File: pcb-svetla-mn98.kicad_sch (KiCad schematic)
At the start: 7 parts, among them J1 TURN PAIRS, J14 P6DC INPUT, J2 MAIN LIGHTS, J3 AUX LIGHTS

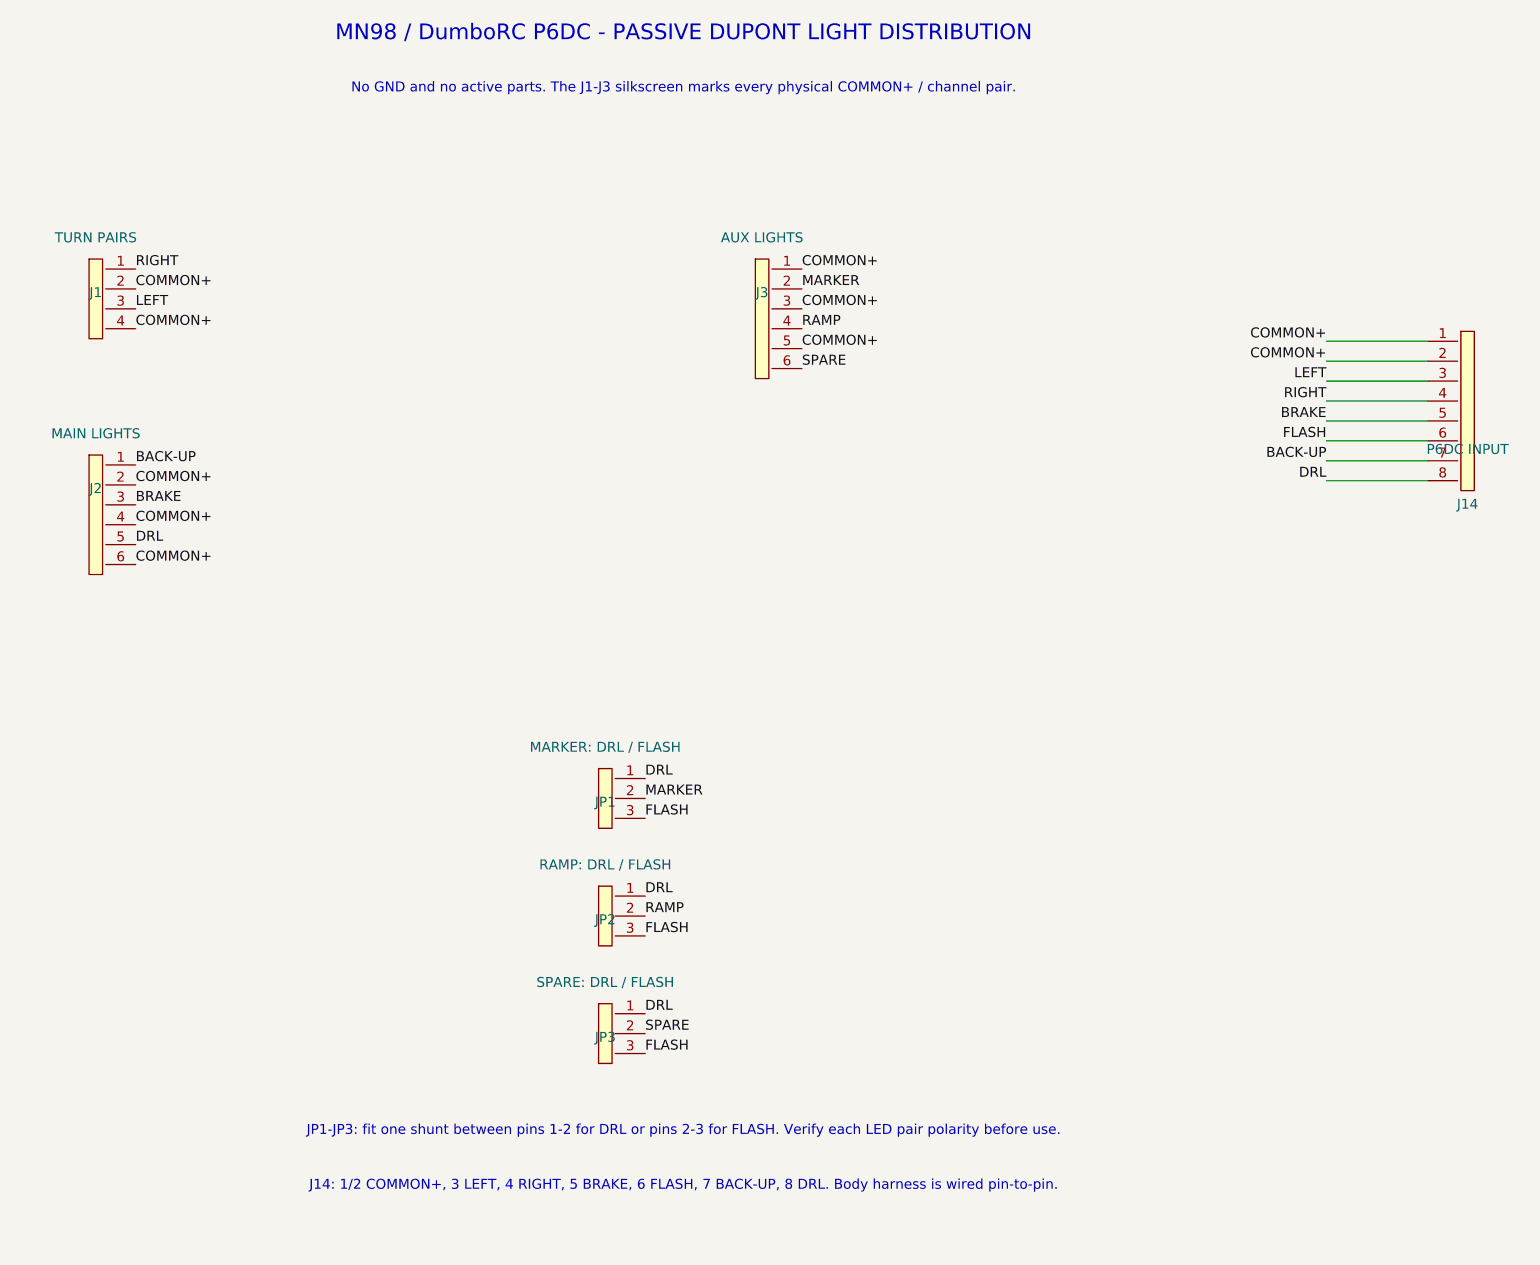
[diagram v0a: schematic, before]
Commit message: Revise body distributor placement
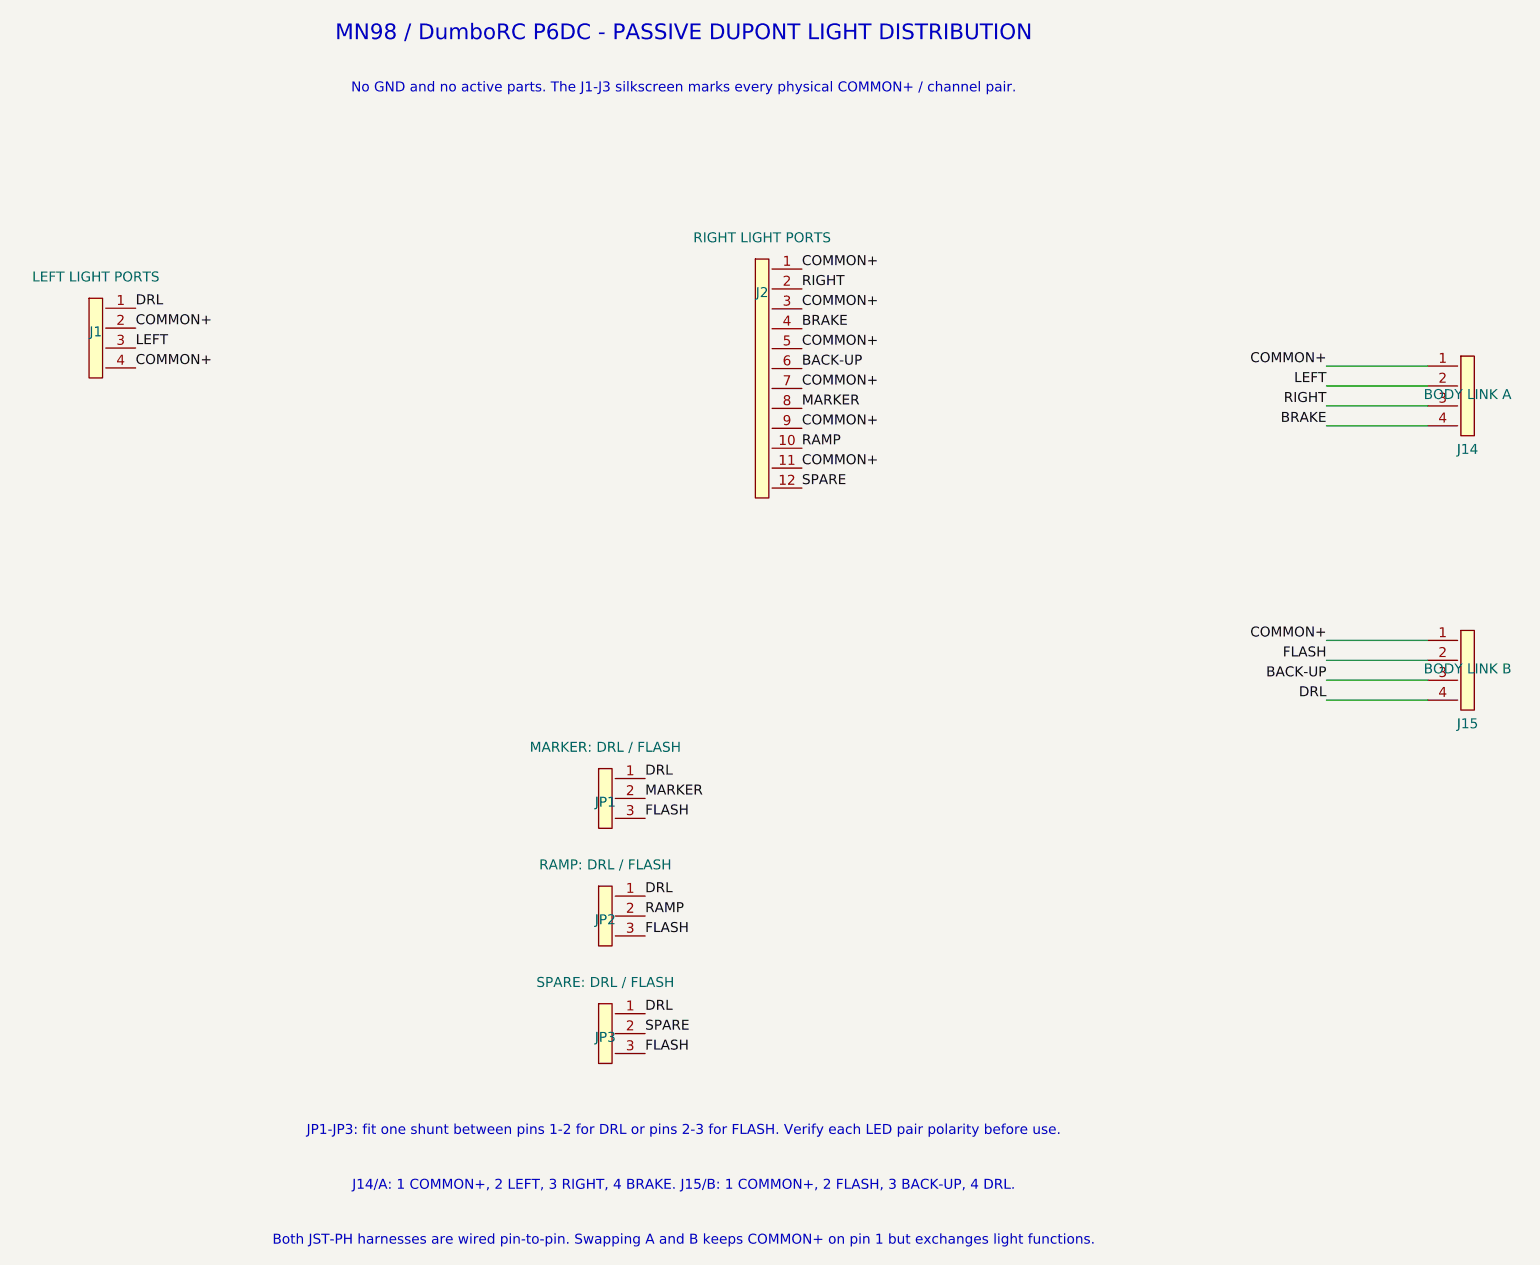
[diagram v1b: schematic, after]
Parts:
- removed J3: AUX LIGHTS, Connector_PinHeader_2.54mm:PinHeader_1x06_P2.54mm_Horizontal, symbol MN98:Conn_01x06
- added J15: BODY LINK B, Connector_JST:JST_PH_S4B-PH-K_1x04_P2.00mm_Horizontal, symbol MN98:Conn_01x04_Input
- J1: value TURN PAIRS -> LEFT LIGHT PORTS
- J14: value P6DC INPUT -> BODY LINK A; footprint Connector_JST:JST_XH_S8B-XH-A_1x08_P2.50mm_Horizontal -> Connector_JST:JST_PH_S4B-PH-K_1x04_P2.00mm_Horizontal; symbol MN98:Conn_01x08_Input -> MN98:Conn_01x04_Input
- J2: value MAIN LIGHTS -> RIGHT LIGHT PORTS; footprint Connector_PinHeader_2.54mm:PinHeader_1x06_P2.54mm_Horizontal -> Connector_PinHeader_2.54mm:PinHeader_1x12_P2.54mm_Horizontal; symbol MN98:Conn_01x06 -> MN98:Conn_01x12
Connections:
- net BACK-UP: now also J2.6 (Pin_6), J15.3 (Pin_3); no longer J14.7 (Pin_7), J2.1 (Pin_1)
- net BRAKE: now also J14.4 (Pin_4), J2.4 (Pin_4); no longer J14.5 (Pin_5), J2.3 (Pin_3)
- net COMMON+: now also J2.1 (Pin_1), J2.11 (Pin_11), J2.3 (Pin_3), J2.5 (Pin_5), J2.7 (Pin_7), J2.9 (Pin_9), J15.1 (Pin_1); no longer J14.2 (Pin_2), J2.2 (Pin_2), J2.4 (Pin_4), J2.6 (Pin_6)
- net DRL: now also J1.1 (Pin_1), J15.4 (Pin_4); no longer J14.8 (Pin_8), J2.5 (Pin_5)
- net FLASH: now also J15.2 (Pin_2); no longer J14.6 (Pin_6)
- net LEFT: now also J14.2 (Pin_2); no longer J14.3 (Pin_3)
- net MARKER: now also J2.8 (Pin_8)
- net RAMP: now also J2.10 (Pin_10)
- net RIGHT: now also J14.3 (Pin_3), J2.2 (Pin_2); no longer J1.1 (Pin_1), J14.4 (Pin_4)
- net SPARE: now also J2.12 (Pin_12)
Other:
- note added: "Both JST-PH harnesses are wired pin-to-pin. Swapping A and B keeps COMMON+ on pin 1 but exchanges light functions."
- note added: "J14/A: 1 COMMON+, 2 LEFT, 3 RIGHT, 4 BRAKE. J15/B: 1 COMMON+, 2 FLASH, 3 BACK-UP, 4 DRL."
- note removed: "J14: 1/2 COMMON+, 3 LEFT, 4 RIGHT, 5 BRAKE, 6 FLASH, 7 BACK-UP, 8 DRL. Body harness is wired pin-to-pin."
- moved on the sheet: J1
